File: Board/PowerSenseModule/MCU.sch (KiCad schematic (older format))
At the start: 14 parts, among them J3 Programming Header, U3 dsPIC33EP32GP502_QFN, U4 MCP2542WFDxMF-SOIC

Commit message: Finalizing Footprints PT B
Have two copies of everything, don't know why. Added NETI to remaining resistors and capacitor. Let's see
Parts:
- R6: footprint (none) -> Resistor_SMD:R_0603_1608Metric_Pad1.05x0.95mm_HandSolder
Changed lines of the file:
@@
 F 0 "R6" H 6168 4546 50  0000 L CNN
 F 1 "10k" H 6168 4455 50  0000 L CNN
-F 2 "" V 6140 4490 50  0001 C CNN
+F 2 "Resistor_SMD:R_0603_1608Metric_Pad1.05x0.95mm_HandSolder" V 6140 4490 50  0001 C CNN
 F 3 "~" H 6100 4500 50  0001 C CNN
 	1    6100 4500

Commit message: Changed C10 from tantalum to ceramic
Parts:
- C10: footprint Capacitor_Tantalum_SMD:CP_EIA-6032-28_Kemet-C_Pad2.25x2.35mm_HandSolder -> Capacitor_SMD:C_0603_1608Metric_Pad1.05x0.95mm_HandSolder
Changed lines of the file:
@@
 F 0 "C10" H 1500 5300 50  0000 L CNN
 F 1 "0.01uF" H 1350 5200 50  0000 L CNN
-F 2 "Capacitor_Tantalum_SMD:CP_EIA-6032-28_Kemet-C_Pad2.25x2.35mm_HandSolder" H 1738 5100 50  0001 C CNN
+F 2 "Capacitor_SMD:C_0603_1608Metric_Pad1.05x0.95mm_HandSolder" H 1738 5100 50  0001 C CNN
 F 3 "~" H 1700 5250 50  0001 C CNN
 	1    1700 5250

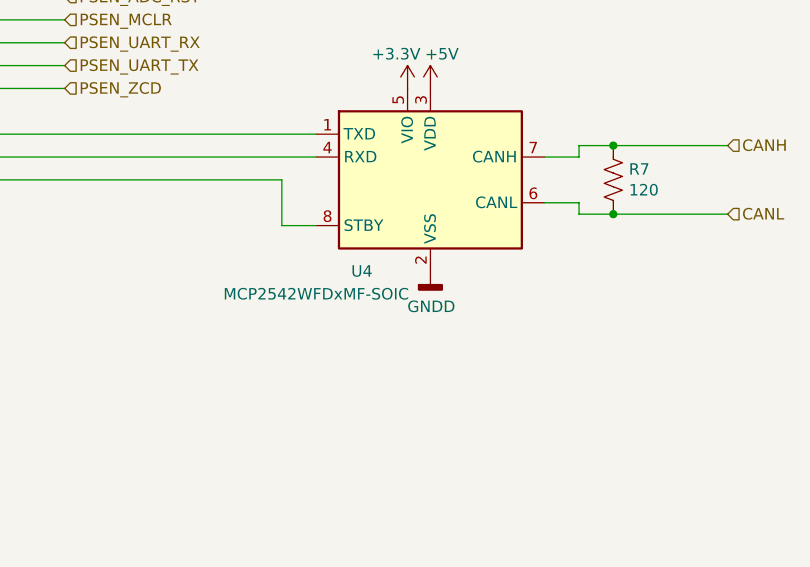
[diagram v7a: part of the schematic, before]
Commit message: Changed can interface lib
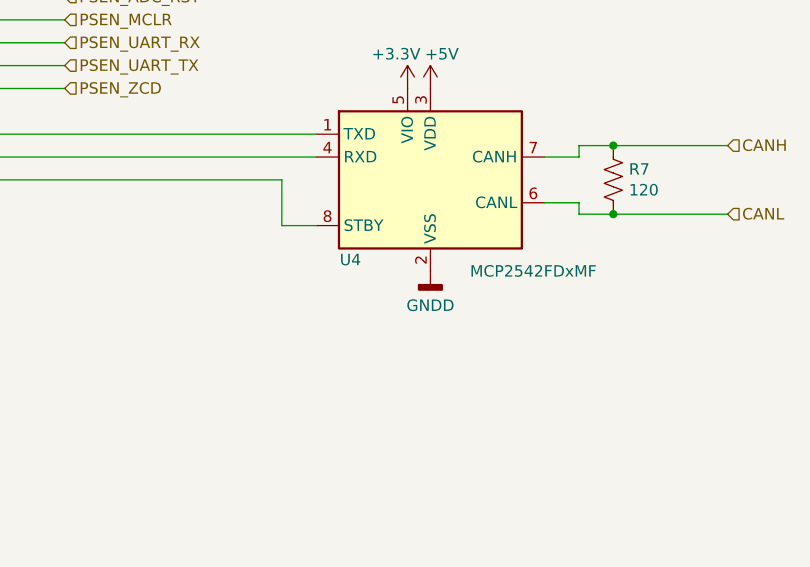
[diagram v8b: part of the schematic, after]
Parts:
- removed U4: MCP2542WFDxMF-SOIC, Package_SO:SOIC-8_3.9x4.9mm_P1.27mm, symbol Interface_CAN_LIN:MCP2542WFDxMF
- added U4: MCP2542FDxMF, Package_DFN_QFN:DFN-8-1EP_3x3mm_P0.65mm_EP1.55x2.4mm, symbol Interface_CAN_LIN:MCP2542FDxMF
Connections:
- net +3V3: now also U4.5 (VIO)
- net +5V: now also U4.3 (VDD)
- net CANH: now also U4.7 (CANH)
- net CANL: now also U4.6 (CANL)
- net GNDD: now also U4.2 (VSS), U4.9 (VSS)
- net at U3.19 (TDI/RP43/RB11): now also U4.1 (TXD)
- net at U3.20 (RPI44/RB12): now also U4.4 (RXD)
- net at U3.21 (RPI45/CTPLS/RB13): now also U4.8 (STBY)
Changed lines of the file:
@@
 Capacitor disconnected when programming\n
-$Comp
-L Interface_CAN_LIN:MCP2542WFDxMF U4
-U 1 1 5D1D10B6
-P 8350 3900
-F 0 "U4" H 8050 3500 50  0000 C CNN
-F 1 "MCP2542WFDxMF-SOIC" H 7850 3400 50  0000 C CNN
-F 2 "Package_SO:SOIC-8_3.9x4.9mm_P1.27mm" H 8350 3400 50  0001 C CIN
-F 3 "http://ww1.microchip.com/downloads/en/DeviceDoc/MCP2542FD-4FD-MCP2542WFD-4WFD-Data-Sheet20005514B.pdf" H 8350 3900 50  0001 C CNN
-	1    8350 3900
-	1    0    0    -1
-$EndComp
 $Comp
 L power:+5V #PWR030
@@
 P 8350 4300
 F 0 "#PWR031" H 8350 4050 50  0001 C CNN
-F 1 "GNDD" H 8354 4145 50  0000 C CNN
+F 1 "GNDD" H 8350 4150 50  0000 C CNN
 F 2 "" H 8350 4300 50  0001 C CNN
 F 3 "" H 8350 4300 50  0001 C CNN
@@
 	1    0    0    -1
 $EndComp
+$Comp
+L Interface_CAN_LIN:MCP2542FDxMF U4
+U 1 1 5D33FB36
+P 8350 3900
+F 0 "U4" H 8000 3550 50  0000 C CNN
+F 1 "MCP2542FDxMF" H 8800 3500 50  0000 C CNN
+F 2 "Package_DFN_QFN:DFN-8-1EP_3x3mm_P0.65mm_EP1.55x2.4mm" H 8350 3400 50  0001 C CIN
+F 3 "http://ww1.microchip.com/downloads/en/DeviceDoc/MCP2542FD-4FD-MCP2542WFD-4WFD-Data-Sheet20005514B.pdf" H 8350 3900 50  0001 C CNN
+	1    8350 3900
+	1    0    0    -1
+$EndComp
